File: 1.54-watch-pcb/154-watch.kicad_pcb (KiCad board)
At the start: 4 copper layers, 50.3 x 33 mm, 67 parts, among them J1 AFC24-S24FIC-00, J2 Conn_01x06_Female, J3 USB_C_Programming, J4 Jack-DC, J5 Conn_01x02_Male, Q1 Si1308, Q2 BC817, Q3 BC817, Q4 Si2301CDS, SW1 RESET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

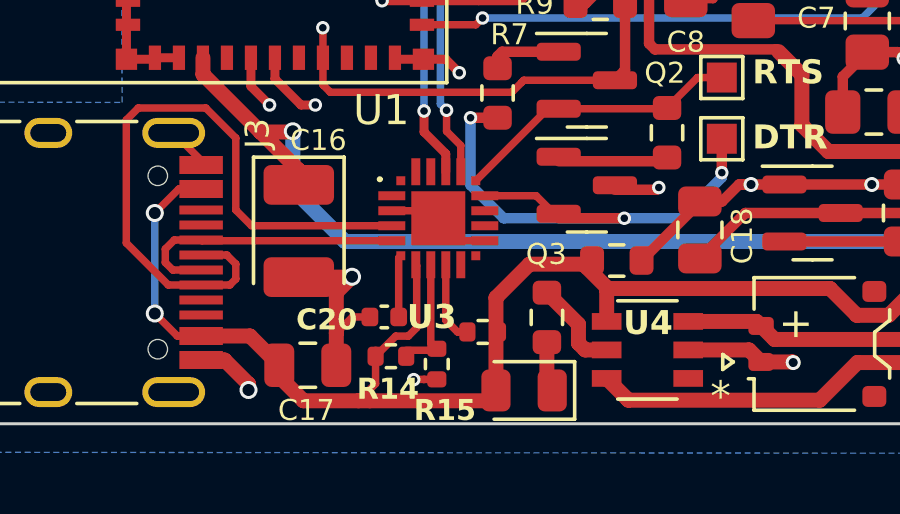
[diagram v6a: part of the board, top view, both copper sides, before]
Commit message: RST is pulled-up now to logic level 3V3
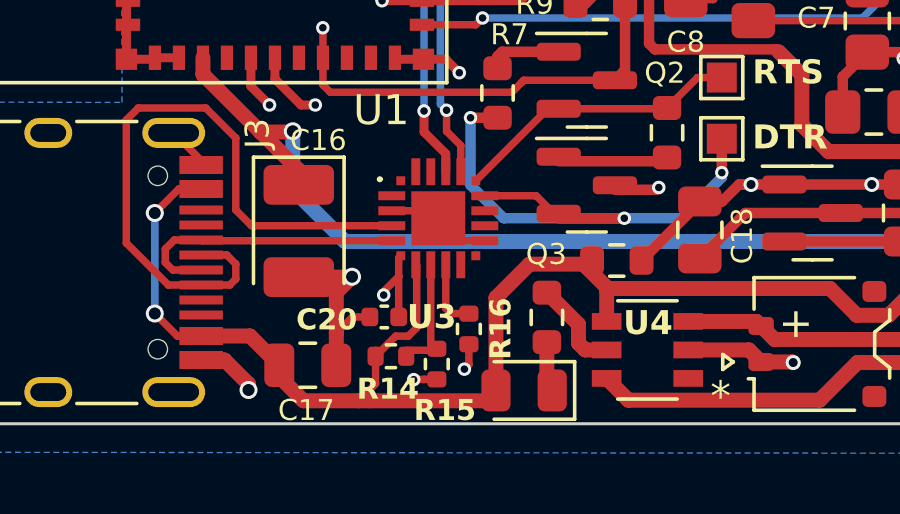
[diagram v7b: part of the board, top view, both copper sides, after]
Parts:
- R16: value 10 K -> 4.7K
- moved R16 0.47 mm to (89.8, 59.3), turned to 90 degrees
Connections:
- C20 pad 1: Net-(U3-VDD) -> UART_VDD
- R16 pad 1: VBUS -> UART_VDD
- U3 pad 6: Net-(U3-VDD) -> UART_VDD
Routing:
- net UART_VDD: track 0.00 -> 7.52 mm, vias 0 -> 2
- net Net-(U3-VDD): track 2.07 -> 0.00 mm
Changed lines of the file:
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@@
   (net 81 "Net-(U3-~{RST})")
   (net 82 "Net-(#FLG01-pwr)")
-  (net 83 "Net-(U3-VDD)")
+  (net 83 "UART_VDD")
   (footprint "Capacitor_SMD:C_0805_2012Metric_Pad1.18x1.45mm_HandSolder" (layer "F.Cu")
     (at 103.27 52.11)
@@
     )
   )
+  (footprint "Resistor_SMD:R_0402_1005Metric" (layer "F.Cu")
+    (at 89.77 59.34 90)
+    (descr "Resistor SMD 0402 (1005 Metric), square (rectangular) end terminal, IPC_7351 nominal, (Body size source: IPC-SM-782 page 72, https://www.pcb-3d.com/wordpress/wp-content/uploads/ipc-sm-782a_amendment_1_and_2.pdf), generated with kicad-footprint-generator")
+    (tags "resistor")
+    (property "LCSC" "C149892")
+    (property "Sheetfile" "154-watch.kicad_sch")
+    (property "Sheetname" "")
+    (property "ki_description" "Resistor, small symbol")
+    (property "ki_keywords" "R resistor")
+    (attr smd)
+    (fp_text reference "R16" (at 0.01 1.06 90) (layer "F.SilkS")
+        (effects (font (size 0.7 0.7) (thickness 0.13) bold))
+    )
+    (fp_text value "4.7K" (at 0 1.17 90) (layer "F.Fab")
+        (effects (font (size 1 1) (thickness 0.15)))
+    )
+    (fp_text user "${REFERENCE}" (at 0 0 90) (layer "F.Fab")
+        (effects (font (size 0.26 0.26) (thickness 0.04)))
+    )
+    (fp_line (start -0.153641 -0.38) (end 0.153641 -0.38)
+      (stroke (width 0.12) (type solid)) (layer "F.SilkS"))
+    (fp_line (start -0.153641 0.38) (end 0.153641 0.38)
+      (stroke (width 0.12) (type solid)) (layer "F.SilkS"))
+    (fp_line (start -0.93 -0.47) (end 0.93 -0.47)
+      (stroke (width 0.05) (type solid)) (layer "F.CrtYd"))
+    (fp_line (start -0.93 0.47) (end -0.93 -0.47)
+      (stroke (width 0.05) (type solid)) (layer "F.CrtYd"))
+    (fp_line (start 0.93 -0.47) (end 0.93 0.47)
+      (stroke (width 0.05) (type solid)) (layer "F.CrtYd"))
+    (fp_line (start 0.93 0.47) (end -0.93 0.47)
+      (stroke (width 0.05) (type solid)) (layer "F.CrtYd"))
+    (fp_line (start -0.525 -0.27) (end 0.525 -0.27)
+      (stroke (width 0.1) (type solid)) (layer "F.Fab"))
+    (fp_line (start -0.525 0.27) (end -0.525 -0.27)
+      (stroke (width 0.1) (type solid)) (layer "F.Fab"))
+    (fp_line (start 0.525 -0.27) (end 0.525 0.27)
+      (stroke (width 0.1) (type solid)) (layer "F.Fab"))
+    (fp_line (start 0.525 0.27) (end -0.525 0.27)
+      (stroke (width 0.1) (type solid)) (layer "F.Fab"))
+    (pad "1" smd roundrect (at -0.51 0 90) (size 0.54 0.64) (layers "F.Cu" "F.Paste" "F.Mask") (roundrect_rratio 0.25)
+      (net 83 "UART_VDD") (pintype "passive"))
+    (pad "2" smd roundrect (at 0.51 0 90) (size 0.54 0.64) (layers "F.Cu" "F.Paste" "F.Mask") (roundrect_rratio 0.25)
+      (net 81 "Net-(U3-~{RST})") (pintype "passive"))
+    (model "${KICAD6_3DMODEL_DIR}/Resistor_SMD.3dshapes/R_0402_1005Metric.wrl"
+      (offset (xyz 0 0 0))
+      (scale (xyz 1 1 1))
+      (rotate (xyz 0 0 0))
+    )
+  )
   (footprint "Resistor_SMD:R_0603_1608Metric" (layer "F.Cu")
     (at 116.245 50.32)
@@
       (stroke (width 0.1) (type solid)) (layer "F.Fab"))
     (pad "1" smd roundrect (at -0.48 0 180) (size 0.56 0.62) (layers "F.Cu" "F.Paste" "F.Mask") (roundrect_rratio 0.25)
-      (net 83 "Net-(U3-VDD)") (pintype "passive"))
+      (net 83 "UART_VDD") (pintype "passive"))
     (pad "2" smd roundrect (at 0.48 0 180) (size 0.56 0.62) (layers "F.Cu" "F.Paste" "F.Mask") (roundrect_rratio 0.25)
       (net 2 "GND") (pintype "passive"))
@@
     )
   )
-  (footprint "Resistor_SMD:R_0402_1005Metric" (layer "F.Cu")
-    (at 90.23 59.44 180)
-    (descr "Resistor SMD 0402 (1005 Metric), square (rectangular) end terminal, IPC_7351 nominal, (Body size source: IPC-SM-782 page 72, https://www.pcb-3d.com/wordpress/wp-content/uploads/ipc-sm-782a_amendment_1_and_2.pdf), generated with kicad-footprint-generator")
-    (tags "resistor")
-    (property "LCSC" "C319933")
-    (property "Sheetfile" "154-watch.kicad_sch")
-    (property "Sheetname" "")
-    (property "ki_description" "Resistor, small symbol")
-    (property "ki_keywords" "R resistor")
-    (attr smd)
-    (fp_text reference "R16" (at 2.06 0.33) (layer "F.SilkS") hide
-        (effects (font (size 0.7 0.7) (thickness 0.13) bold))
-    )
-    (fp_text value "10 K" (at 0 1.17) (layer "F.Fab")
-        (effects (font (size 1 1) (thickness 0.15)))
-    )
-    (fp_text user "${REFERENCE}" (at 0 0) (layer "F.Fab")
-        (effects (font (size 0.26 0.26) (thickness 0.04)))
-    )
-    (fp_line (start -0.153641 -0.38) (end 0.153641 -0.38)
-      (stroke (width 0.12) (type solid)) (layer "F.SilkS"))
-    (fp_line (start -0.153641 0.38) (end 0.153641 0.38)
-      (stroke (width 0.12) (type solid)) (layer "F.SilkS"))
-    (fp_line (start -0.93 -0.47) (end 0.93 -0.47)
-      (stroke (width 0.05) (type solid)) (layer "F.CrtYd"))
-    (fp_line (start -0.93 0.47) (end -0.93 -0.47)
-      (stroke (width 0.05) (type solid)) (layer "F.CrtYd"))
-    (fp_line (start 0.93 -0.47) (end 0.93 0.47)
-      (stroke (width 0.05) (type solid)) (layer "F.CrtYd"))
-    (fp_line (start 0.93 0.47) (end -0.93 0.47)
-      (stroke (width 0.05) (type solid)) (layer "F.CrtYd"))
-    (fp_line (start -0.525 -0.27) (end 0.525 -0.27)
-      (stroke (width 0.1) (type solid)) (layer "F.Fab"))
-    (fp_line (start -0.525 0.27) (end -0.525 -0.27)
-      (stroke (width 0.1) (type solid)) (layer "F.Fab"))
-    (fp_line (start 0.525 -0.27) (end 0.525 0.27)
-      (stroke (width 0.1) (type solid)) (layer "F.Fab"))
-    (fp_line (start 0.525 0.27) (end -0.525 0.27)
-      (stroke (width 0.1) (type solid)) (layer "F.Fab"))
-    (pad "1" smd roundrect (at -0.51 0 180) (size 0.54 0.64) (layers "F.Cu" "F.Paste" "F.Mask") (roundrect_rratio 0.25)
-      (net 3 "VBUS") (pintype "passive"))
-    (pad "2" smd roundrect (at 0.51 0 180) (size 0.54 0.64) (layers "F.Cu" "F.Paste" "F.Mask") (roundrect_rratio 0.25)
-      (net 81 "Net-(U3-~{RST})") (pintype "passive"))
-    (model "${KICAD6_3DMODEL_DIR}/Resistor_SMD.3dshapes/R_0402_1005Metric.wrl"
-      (offset (xyz 0 0 0))
-      (scale (xyz 1 1 1))
-      (rotate (xyz 0 0 0))
-    )
-  )
   (footprint "footprint:CP2102NA02GQFN20" (layer "F.Cu")
     (at 88.75 55.65)
@@
       (net 37 "Net-(U3-D-)") (pinfunction "D-") (pintype "bidirectional"))
     (pad "6" smd rect (at -1.25 1.25) (size 0.3 0.3) (layers "F.Cu" "F.Paste" "F.Mask")
-      (net 83 "Net-(U3-VDD)") (pinfunction "VDD") (pintype "power_in"))
+      (net 83 "UART_VDD") (pinfunction "VDD") (pintype "power_in"))
     (pad "7" smd rect (at -0.75 1.55) (size 0.3 0.9) (layers "F.Cu" "F.Paste" "F.Mask")
       (net 3 "VBUS") (pinfunction "VREGIN") (pintype "power_in"))
@@
   (segment (start 88.5 59.8) (end 88.7 60) (width 0.25) (layer "F.Cu") (net 73))
   (segment (start 88.5 57.2) (end 88.5 59.8) (width 0.25) (layer "F.Cu") (net 73))
-  (segment (start 89 59.05) (end 89.39 59.44) (width 0.25) (layer "F.Cu") (net 81))
-  (segment (start 89.39 59.44) (end 89.72 59.44) (width 0.25) (layer "F.Cu") (net 81))
-  (segment (start 89 57.2) (end 89 59.05) (width 0.25) (layer "F.Cu") (net 81))
+  (segment (start 89.77 58.83) (end 89.18 58.83) (width 0.25) (layer "F.Cu") (net 81))
+  (segment (start 89 57.2) (end 89 58.65) (width 0.25) (layer "F.Cu") (net 81))
+  (segment (start 89.18 58.83) (end 89 58.65) (width 0.25) (layer "F.Cu") (net 81))
   (segment (start 91.61 30.49) (end 91.575 30.525) (width 0.35) (layer "F.Cu") (net 82))
   (segment (start 92.30625 34.2875) (end 92.30625 32.40125) (width 0.35) (layer "F.Cu") (net 82))
@@
   (segment (start 82.18 30.18) (end 91.3 30.18) (width 0.35) (layer "F.Cu") (net 82))
   (segment (start 81.47 30.89) (end 82.18 30.18) (width 0.35) (layer "F.Cu") (net 82))
-  (segment (start 87.43 58.94) (end 87.43 56.97) (width 0.25) (layer "F.Cu") (net 83))
+  (segment (start 86.93 58.09) (end 87.43 57.59) (width 0.25) (layer "F.Cu") (net 83))
+  (segment (start 87.43 57.59) (end 87.43 56.97) (width 0.25) (layer "F.Cu") (net 83))
   (segment (start 87.43 56.97) (end 87.5 56.9) (width 0.25) (layer "F.Cu") (net 83))
+  (segment (start 89.77 60.53) (end 89.62 60.68) (width 0.25) (layer "F.Cu") (net 83))
+  (segment (start 86.93 58.21) (end 86.93 58.09) (width 0.25) (layer "F.Cu") (net 83))
+  (segment (start 87.43 58.94) (end 87.43 57.59) (width 0.25) (layer "F.Cu") (net 83))
+  (segment (start 89.77 59.85) (end 89.77 60.53) (width 0.25) (layer "F.Cu") (net 83))
+  (segment (start 86.93 58.21) (end 86.92 58.2) (width 0.25) (layer "F.Cu") (net 83))
+  (via (at 86.93 58.21) (size 0.45) (drill 0.25) (layers "F.Cu" "B.Cu") (net 83))
+  (via (at 89.62 60.68) (size 0.45) (drill 0.25) (layers "F.Cu" "B.Cu") (net 83))
+  (segment (start 89.4 60.68) (end 86.93 58.21) (width 0.25) (layer "In2.Cu") (net 83))
+  (segment (start 89.62 60.68) (end 89.4 60.68) (width 0.25) (layer "In2.Cu") (net 83))
   (zone (net 2) (net_name "GND") (layer "In1.Cu") (hatch edge 0.508)
     (connect_pads (clearance 0.508))
